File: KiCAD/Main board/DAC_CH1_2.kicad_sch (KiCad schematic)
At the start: 73 parts, among them U1 LM4562, U1 PCM1789, U3 OPA1632DR, U4 OPA1632DR

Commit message: Worked on main board SCH
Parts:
- removed C11, C20, C5: 22uF, Capacitor_THT:CP_Radial_D5.0mm_P2.00mm, symbol Device:C_Polarized
- removed C15, C7: 100n, Capacitor_SMD:C_0402_1005Metric, symbol Device:C
- added C11, C5: 100n, Capacitor_SMD:C_0402_1005Metric, symbol Device:C
- added C15, C39, C7: 22uF, Capacitor_THT:CP_Radial_D5.0mm_P2.00mm, symbol Device:C_Polarized
- C18: footprint Capacitor_SMD:C_0805_2012Metric -> Capacitor_SMD:C_0402_1005Metric
- C29, C30: value 2.2n -> 2n2
- R17, R18, R19, R20: value 4.7k -> 4k7
- R25, R27: value 4.3K -> 4k3
- R26, R28: value 4.3k -> 4k3
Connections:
- net +3.3V: now also C39.1, C5.1; no longer C6.1
- net GND: now also C10.1, C19.1, C11.2, C15.2, C39.2, C5.2, C7.2; no longer C10.2, C19.2
- net at R6.2, U4.3 (V+): now also C11.1, C15.1; no longer C19.1
- net at C8.2, R4.1, U3.6 (V-): now also C10.2
- net at R3.2, U3.3 (V+): now also C6.1, C7.1; no longer C10.1
- net at C16.2, R7.1, U4.6 (V-): now also C19.2
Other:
- moved on the sheet: C24, R27, R31, R32, R33, R34

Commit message: Worked on main board and added nettie 0.3mm
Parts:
- NT1, NT2: footprint NetTie:NetTie-2_SMD_Pad0.5mm -> Audio-DSP:NetTie-2_SMD_Pad0.3mm
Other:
- note removed: "Update to 0.3mm"
- moved on the sheet: R17, R18, R19, R20
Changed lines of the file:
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@@
     (stroke (width 0) (type default))
   )
-  (wire (pts (xy 135.89 163.83) (xy 172.72 163.83))
+  (wire (pts (xy 140.97 163.83) (xy 172.72 163.83))
     (stroke (width 0) (type default))
   )
@@
     (stroke (width 0) (type default))
   )
-  (wire (pts (xy 135.89 208.28) (xy 172.72 208.28))
+  (wire (pts (xy 140.97 208.28) (xy 172.72 208.28))
     (stroke (width 0) (type default))
   )
@@
     (stroke (width 0) (type default))
   )
-  (wire (pts (xy 128.27 208.28) (xy 127 208.28))
+  (wire (pts (xy 133.35 208.28) (xy 127 208.28))
     (stroke (width 0) (type default))
   )
@@
     (stroke (width 0) (type default))
   )
-  (wire (pts (xy 135.89 66.04) (xy 172.72 66.04))
+  (wire (pts (xy 140.97 66.04) (xy 172.72 66.04))
     (stroke (width 0) (type default))
   )
@@
     (stroke (width 0) (type default))
   )
+  (wire (pts (xy 46.99 80.01) (xy 48.26 80.01))
+    (stroke (width 0) (type default))
+  )
   (wire (pts (xy 24.13 270.51) (xy 24.13 271.78))
     (stroke (width 0) (type default))
@@
     (stroke (width 0) (type default))
   )
-  (wire (pts (xy 127 163.83) (xy 128.27 163.83))
+  (wire (pts (xy 127 163.83) (xy 133.35 163.83))
     (stroke (width 0) (type default))
   )
@@
     (stroke (width 0) (type default))
   )
-  (wire (pts (xy 135.89 110.49) (xy 172.72 110.49))
+  (wire (pts (xy 139.7 110.49) (xy 172.72 110.49))
     (stroke (width 0) (type default))
   )
@@
     (stroke (width 0) (type default))
   )
-  (wire (pts (xy 128.27 110.49) (xy 127 110.49))
+  (wire (pts (xy 132.08 110.49) (xy 127 110.49))
     (stroke (width 0) (type default))
   )
@@
     (stroke (width 0) (type default))
   )
-  (wire (pts (xy 127 66.04) (xy 128.27 66.04))
+  (wire (pts (xy 127 66.04) (xy 133.35 66.04))
     (stroke (width 0) (type default))
   )
@@
   (wire (pts (xy 63.5 48.26) (xy 72.39 48.26))
     (stroke (width 0) (type default))
-  )
-  (text "Update to 0.3mm" (at 163.83 53.34 0)
-    (effects (font (size 1.27 1.27) bold) (justify left bottom))
-  )
-  (text "Update to 0.3mm" (at 165.1 152.4 0)
-    (effects (font (size 1.27 1.27) bold) (justify left bottom))
   )
   (text "Place nettie at output connector" (at 163.83 55.88 0)
@@
     )
   )
-  (symbol (lib_id "Device:R") (at 132.08 110.49 90) (unit 1)
-    (in_bom yes) (on_board yes) (dnp no)
-    (property "Reference" "R18" (at 132.08 107.95 90)
-      (effects (font (size 1.27 1.27)))
-    )
-    (property "Value" "4k7" (at 132.08 110.49 90)
-      (effects (font (size 1.27 1.27)))
-    )
-    (property "Footprint" "Resistor_SMD:R_0805_2012Metric" (at 132.08 112.268 90)
-      (effects (font (size 1.27 1.27)) hide)
-    )
-    (property "Datasheet" "~" (at 132.08 110.49 0)
+  (symbol (lib_id "Device:R") (at 135.89 110.49 90) (unit 1)
+    (in_bom yes) (on_board yes) (dnp no)
+    (property "Reference" "R18" (at 135.89 107.95 90)
+      (effects (font (size 1.27 1.27)))
+    )
+    (property "Value" "4k7" (at 135.89 110.49 90)
+      (effects (font (size 1.27 1.27)))
+    )
+    (property "Footprint" "Resistor_SMD:R_0805_2012Metric" (at 135.89 112.268 90)
+      (effects (font (size 1.27 1.27)) hide)
+    )
+    (property "Datasheet" "~" (at 135.89 110.49 0)
       (effects (font (size 1.27 1.27)) hide)
     )
@@
     )
   )
-  (symbol (lib_id "Device:R") (at 132.08 208.28 90) (unit 1)
-    (in_bom yes) (on_board yes) (dnp no)
-    (property "Reference" "R20" (at 132.08 205.74 90)
-      (effects (font (size 1.27 1.27)))
-    )
-    (property "Value" "4k7" (at 132.08 208.28 90)
-      (effects (font (size 1.27 1.27)))
-    )
-    (property "Footprint" "Resistor_SMD:R_0805_2012Metric" (at 132.08 210.058 90)
-      (effects (font (size 1.27 1.27)) hide)
-    )
-    (property "Datasheet" "~" (at 132.08 208.28 0)
+  (symbol (lib_id "Device:R") (at 137.16 208.28 90) (unit 1)
+    (in_bom yes) (on_board yes) (dnp no)
+    (property "Reference" "R20" (at 137.16 205.74 90)
+      (effects (font (size 1.27 1.27)))
+    )
+    (property "Value" "4k7" (at 137.16 208.28 90)
+      (effects (font (size 1.27 1.27)))
+    )
+    (property "Footprint" "Resistor_SMD:R_0805_2012Metric" (at 137.16 210.058 90)
+      (effects (font (size 1.27 1.27)) hide)
+    )
+    (property "Datasheet" "~" (at 137.16 208.28 0)
       (effects (font (size 1.27 1.27)) hide)
     )
@@
     )
   )
-  (symbol (lib_id "Device:R") (at 132.08 66.04 90) (unit 1)
-    (in_bom yes) (on_board yes) (dnp no)
-    (property "Reference" "R17" (at 132.08 63.5 90)
-      (effects (font (size 1.27 1.27)))
-    )
-    (property "Value" "4k7" (at 132.08 66.04 90)
-      (effects (font (size 1.27 1.27)))
-    )
-    (property "Footprint" "Resistor_SMD:R_0805_2012Metric" (at 132.08 67.818 90)
-      (effects (font (size 1.27 1.27)) hide)
-    )
-    (property "Datasheet" "~" (at 132.08 66.04 0)
+  (symbol (lib_id "Device:R") (at 137.16 66.04 90) (unit 1)
+    (in_bom yes) (on_board yes) (dnp no)
+    (property "Reference" "R17" (at 137.16 63.5 90)
+      (effects (font (size 1.27 1.27)))
+    )
+    (property "Value" "4k7" (at 137.16 66.04 90)
+      (effects (font (size 1.27 1.27)))
+    )
+    (property "Footprint" "Resistor_SMD:R_0805_2012Metric" (at 137.16 67.818 90)
+      (effects (font (size 1.27 1.27)) hide)
+    )
+    (property "Datasheet" "~" (at 137.16 66.04 0)
       (effects (font (size 1.27 1.27)) hide)
     )
@@
       (effects (font (size 1.27 1.27)) (justify right))
     )
-    (property "Footprint" "NetTie:NetTie-2_SMD_Pad0.5mm" (at 160.02 147.32 0)
+    (property "Footprint" "Audio-DSP:NetTie-2_SMD_Pad0.3mm" (at 160.02 147.32 0)
       (effects (font (size 1.27 1.27)) hide)
     )
@@
     )
   )
-  (symbol (lib_id "Device:R") (at 132.08 163.83 90) (unit 1)
-    (in_bom yes) (on_board yes) (dnp no)
-    (property "Reference" "R19" (at 132.08 161.29 90)
-      (effects (font (size 1.27 1.27)))
-    )
-    (property "Value" "4k7" (at 132.08 163.83 90)
-      (effects (font (size 1.27 1.27)))
-    )
-    (property "Footprint" "Resistor_SMD:R_0805_2012Metric" (at 132.08 165.608 90)
-      (effects (font (size 1.27 1.27)) hide)
-    )
-    (property "Datasheet" "~" (at 132.08 163.83 0)
+  (symbol (lib_id "Device:R") (at 137.16 163.83 90) (unit 1)
+    (in_bom yes) (on_board yes) (dnp no)
+    (property "Reference" "R19" (at 137.16 161.29 90)
+      (effects (font (size 1.27 1.27)))
+    )
+    (property "Value" "4k7" (at 137.16 163.83 90)
+      (effects (font (size 1.27 1.27)))
+    )
+    (property "Footprint" "Resistor_SMD:R_0805_2012Metric" (at 137.16 165.608 90)
+      (effects (font (size 1.27 1.27)) hide)
+    )
+    (property "Datasheet" "~" (at 137.16 163.83 0)
       (effects (font (size 1.27 1.27)) hide)
     )
@@
     )
   )
-  (symbol (lib_id "power:+3.3V") (at 48.26 80.01 90) (unit 1)
-    (in_bom yes) (on_board yes) (dnp no)
-    (property "Reference" "#PWR0137" (at 52.07 80.01 0)
-      (effects (font (size 1.27 1.27)) hide)
-    )
-    (property "Value" "+3.3V" (at 44.45 83.82 0)
-      (effects (font (size 1.27 1.27)) (justify left))
-    )
-    (property "Footprint" "" (at 48.26 80.01 0)
-      (effects (font (size 1.27 1.27)) hide)
-    )
-    (property "Datasheet" "" (at 48.26 80.01 0)
+  (symbol (lib_id "power:+3.3V") (at 46.99 80.01 90) (unit 1)
+    (in_bom yes) (on_board yes) (dnp no)
+    (property "Reference" "#PWR0137" (at 50.8 80.01 0)
+      (effects (font (size 1.27 1.27)) hide)
+    )
+    (property "Value" "+3.3V" (at 43.18 83.82 0)
+      (effects (font (size 1.27 1.27)) (justify left))
+    )
+    (property "Footprint" "" (at 46.99 80.01 0)
+      (effects (font (size 1.27 1.27)) hide)
+    )
+    (property "Datasheet" "" (at 46.99 80.01 0)
       (effects (font (size 1.27 1.27)) hide)
     )
@@
       (effects (font (size 1.27 1.27)) (justify right))
     )
-    (property "Footprint" "NetTie:NetTie-2_SMD_Pad0.5mm" (at 158.75 48.26 0)
-      (effects (font (size 1.27 1.27)) hide)
-    )
+    (property "Footprint" "Audio-DSP:NetTie-2_SMD_Pad0.3mm" (at 158.75 48.26 0)
+      (effects (font (size 1.27 1.27)) hide)
+    )

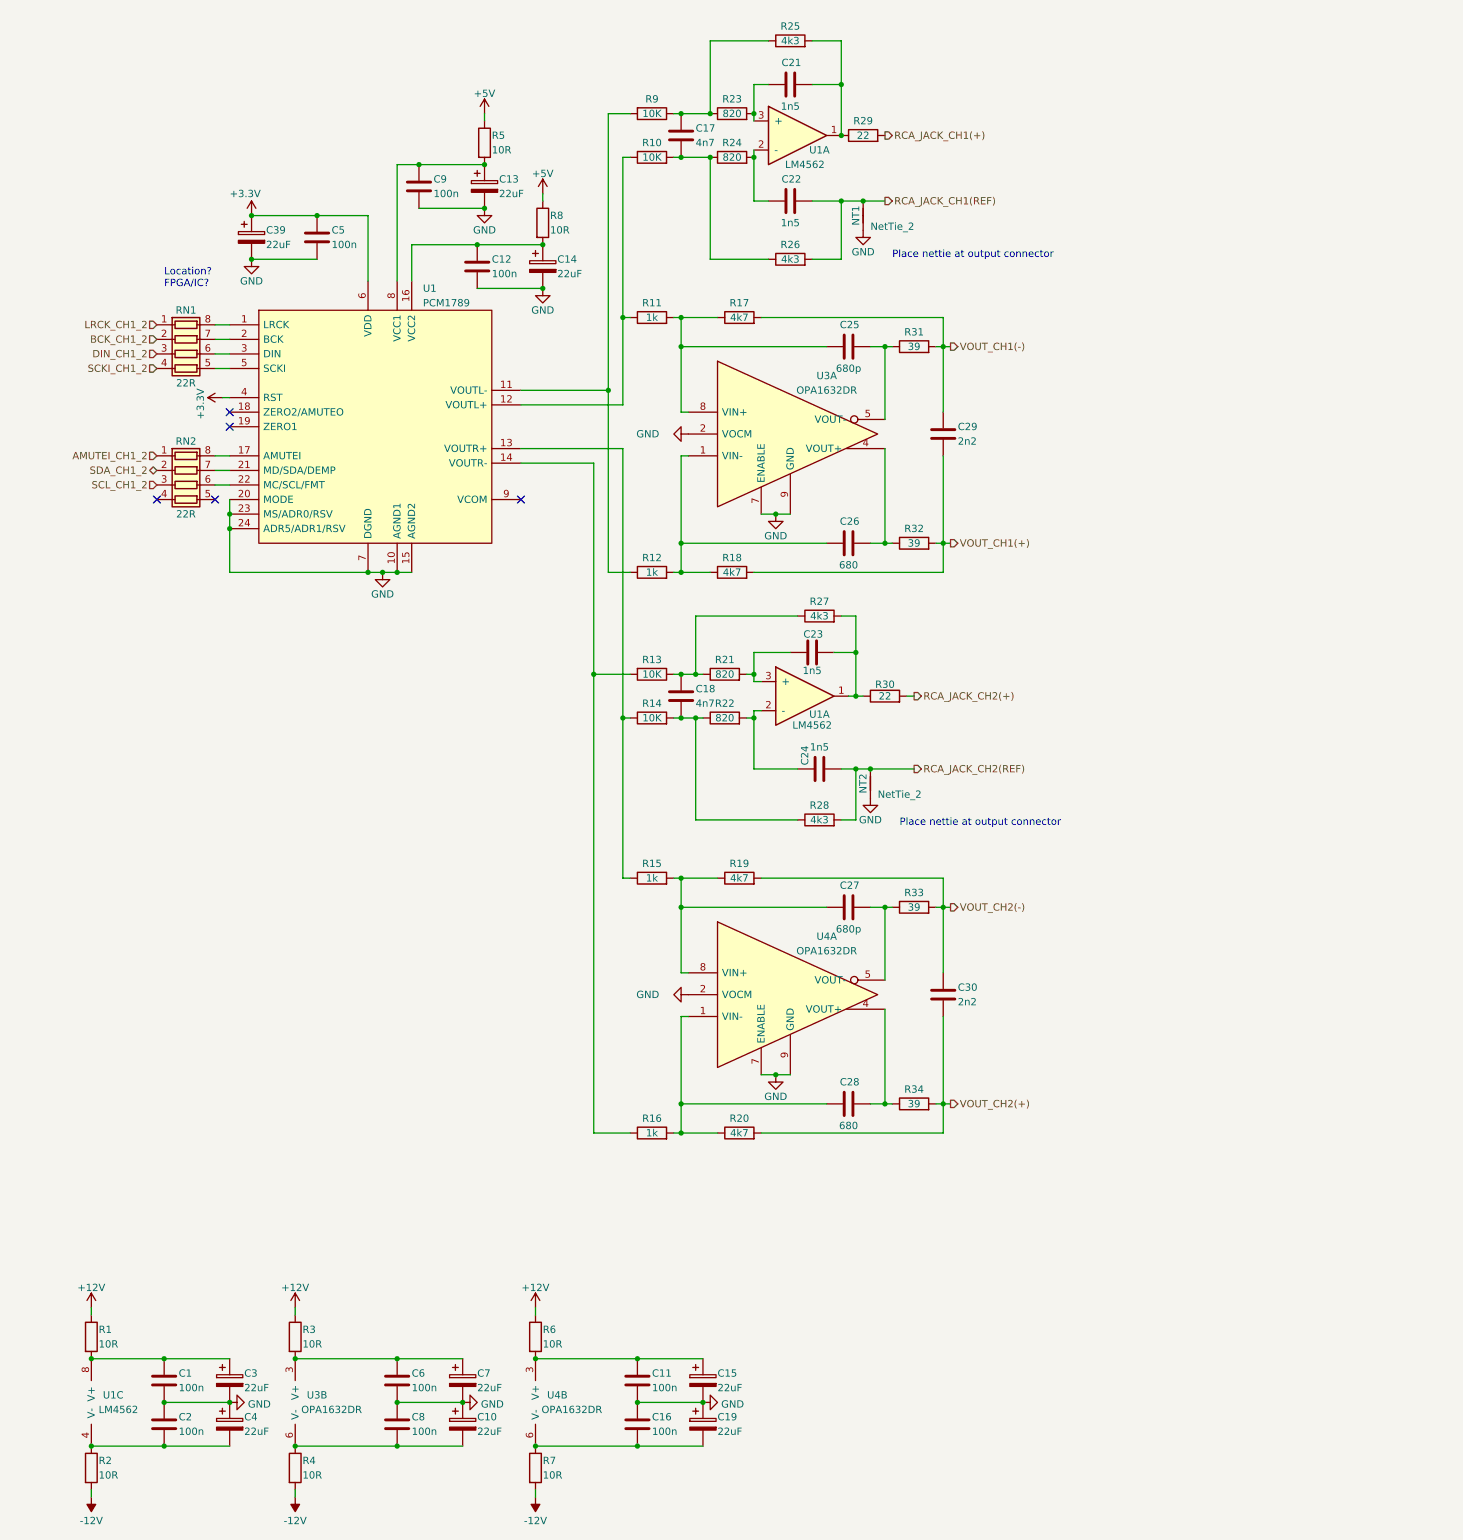
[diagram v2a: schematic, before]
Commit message: Worked on SDD, main board schematic and LTspice discrete linear regulator
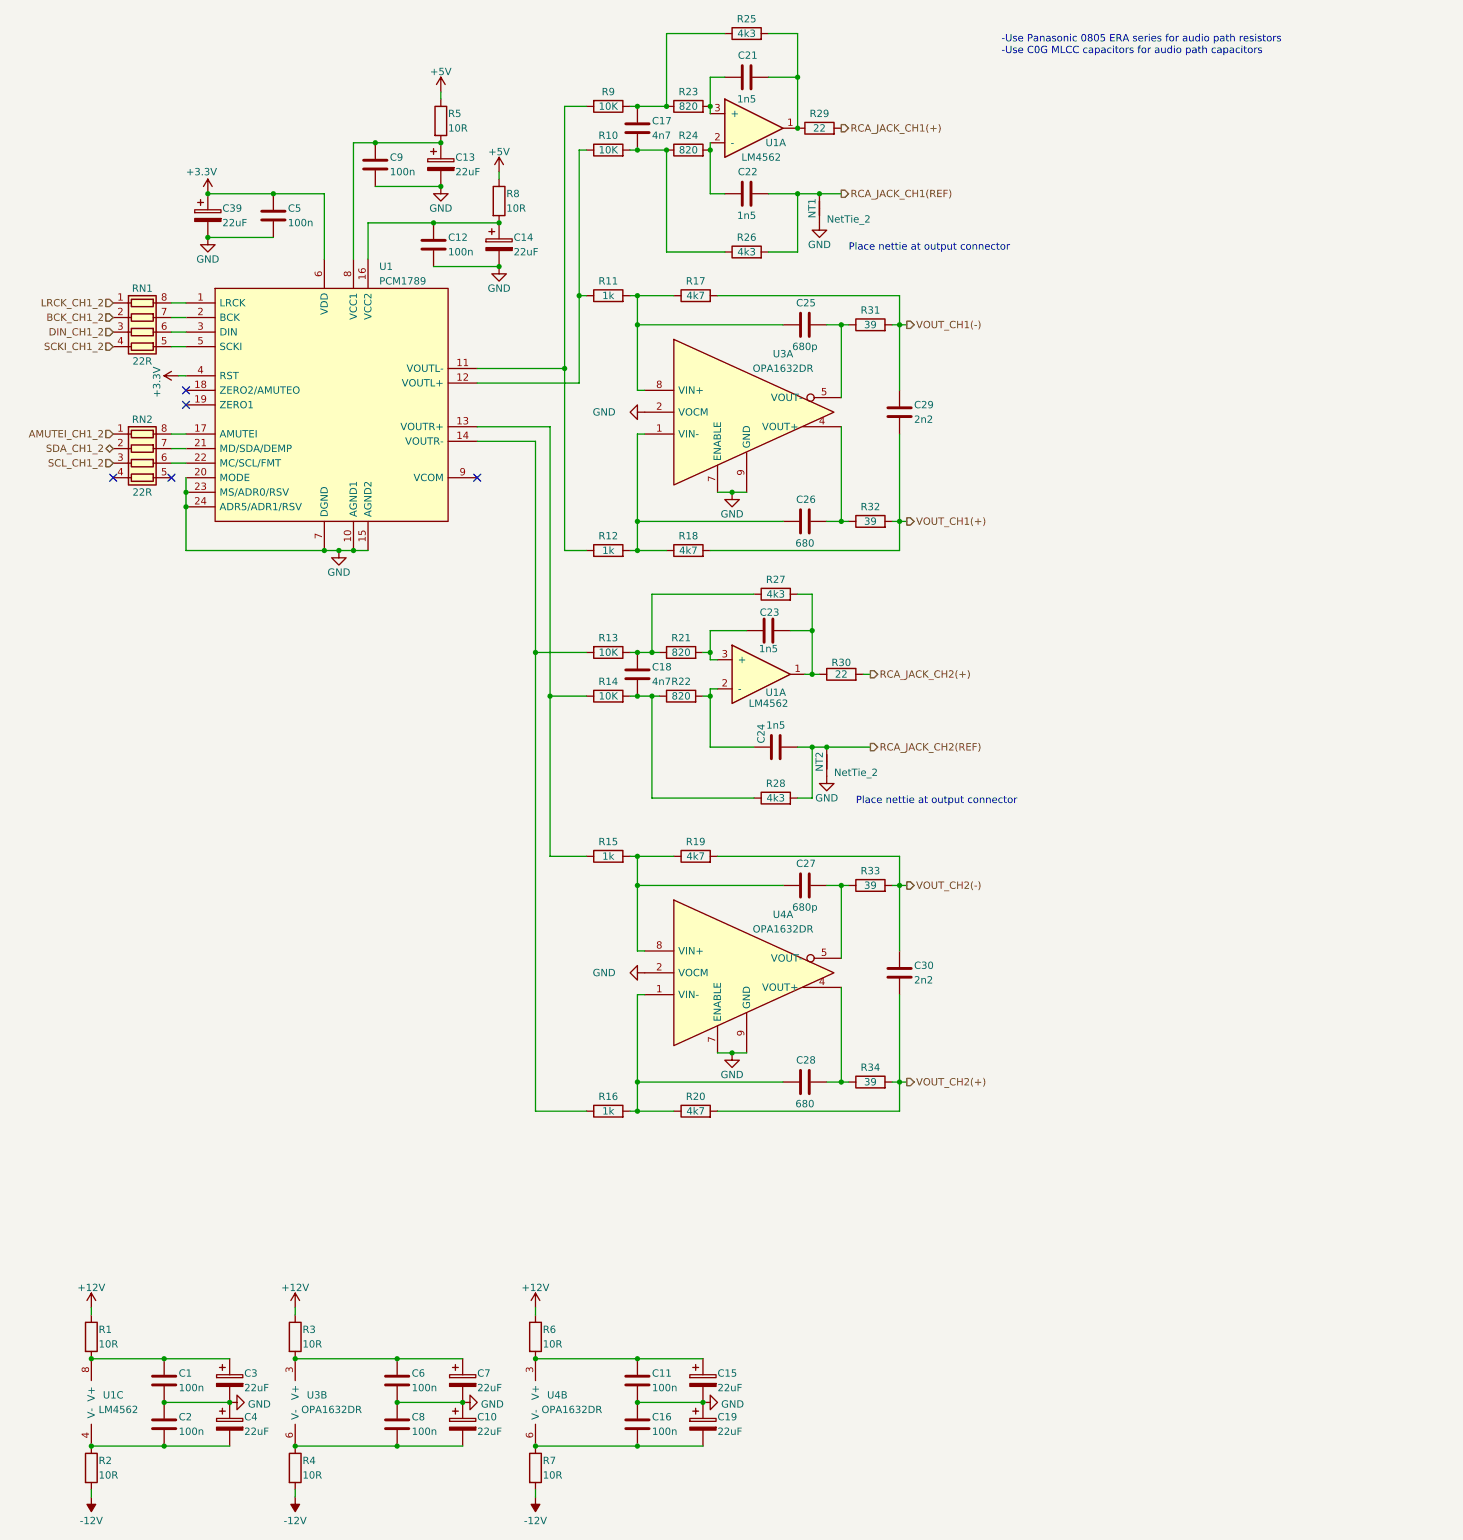
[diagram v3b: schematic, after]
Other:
- note added: "-Use Panasonic 0805 ERA series for audio path resistors -Use C0G MLCC capacitors for audio path capacitors"
- note removed: "Location? FPGA/IC?"
- moved on the sheet: C12, C13, C14, C17, C18, C21, C22, C23, C24, C25, C26, C27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
